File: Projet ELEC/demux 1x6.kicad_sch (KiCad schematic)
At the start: 4 parts, among them U1 74LS04, U2 74LS21, U3 74LS21, U4 74LS21

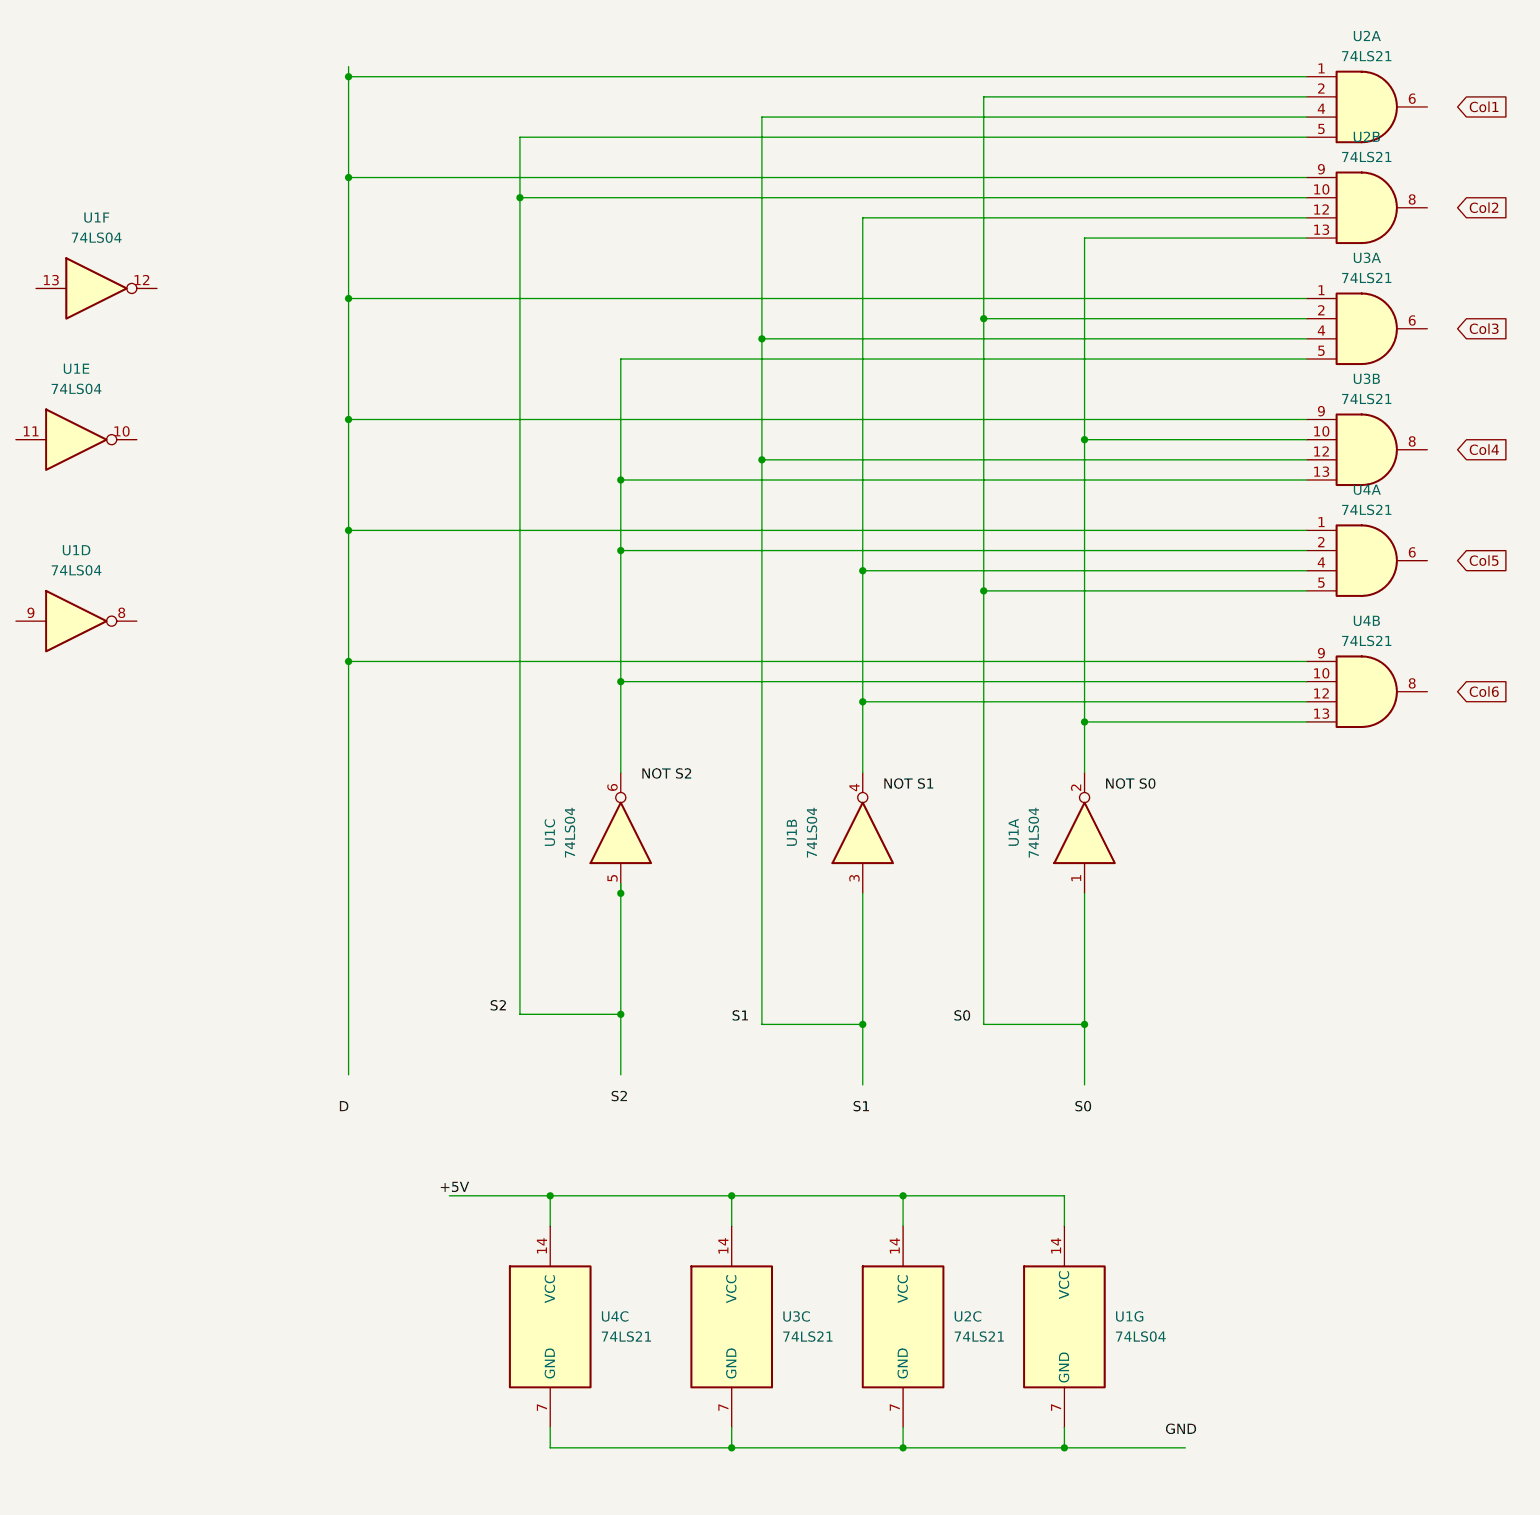
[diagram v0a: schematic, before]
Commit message: corrected around 60 errors, removed a 74ls04, and many other improvements
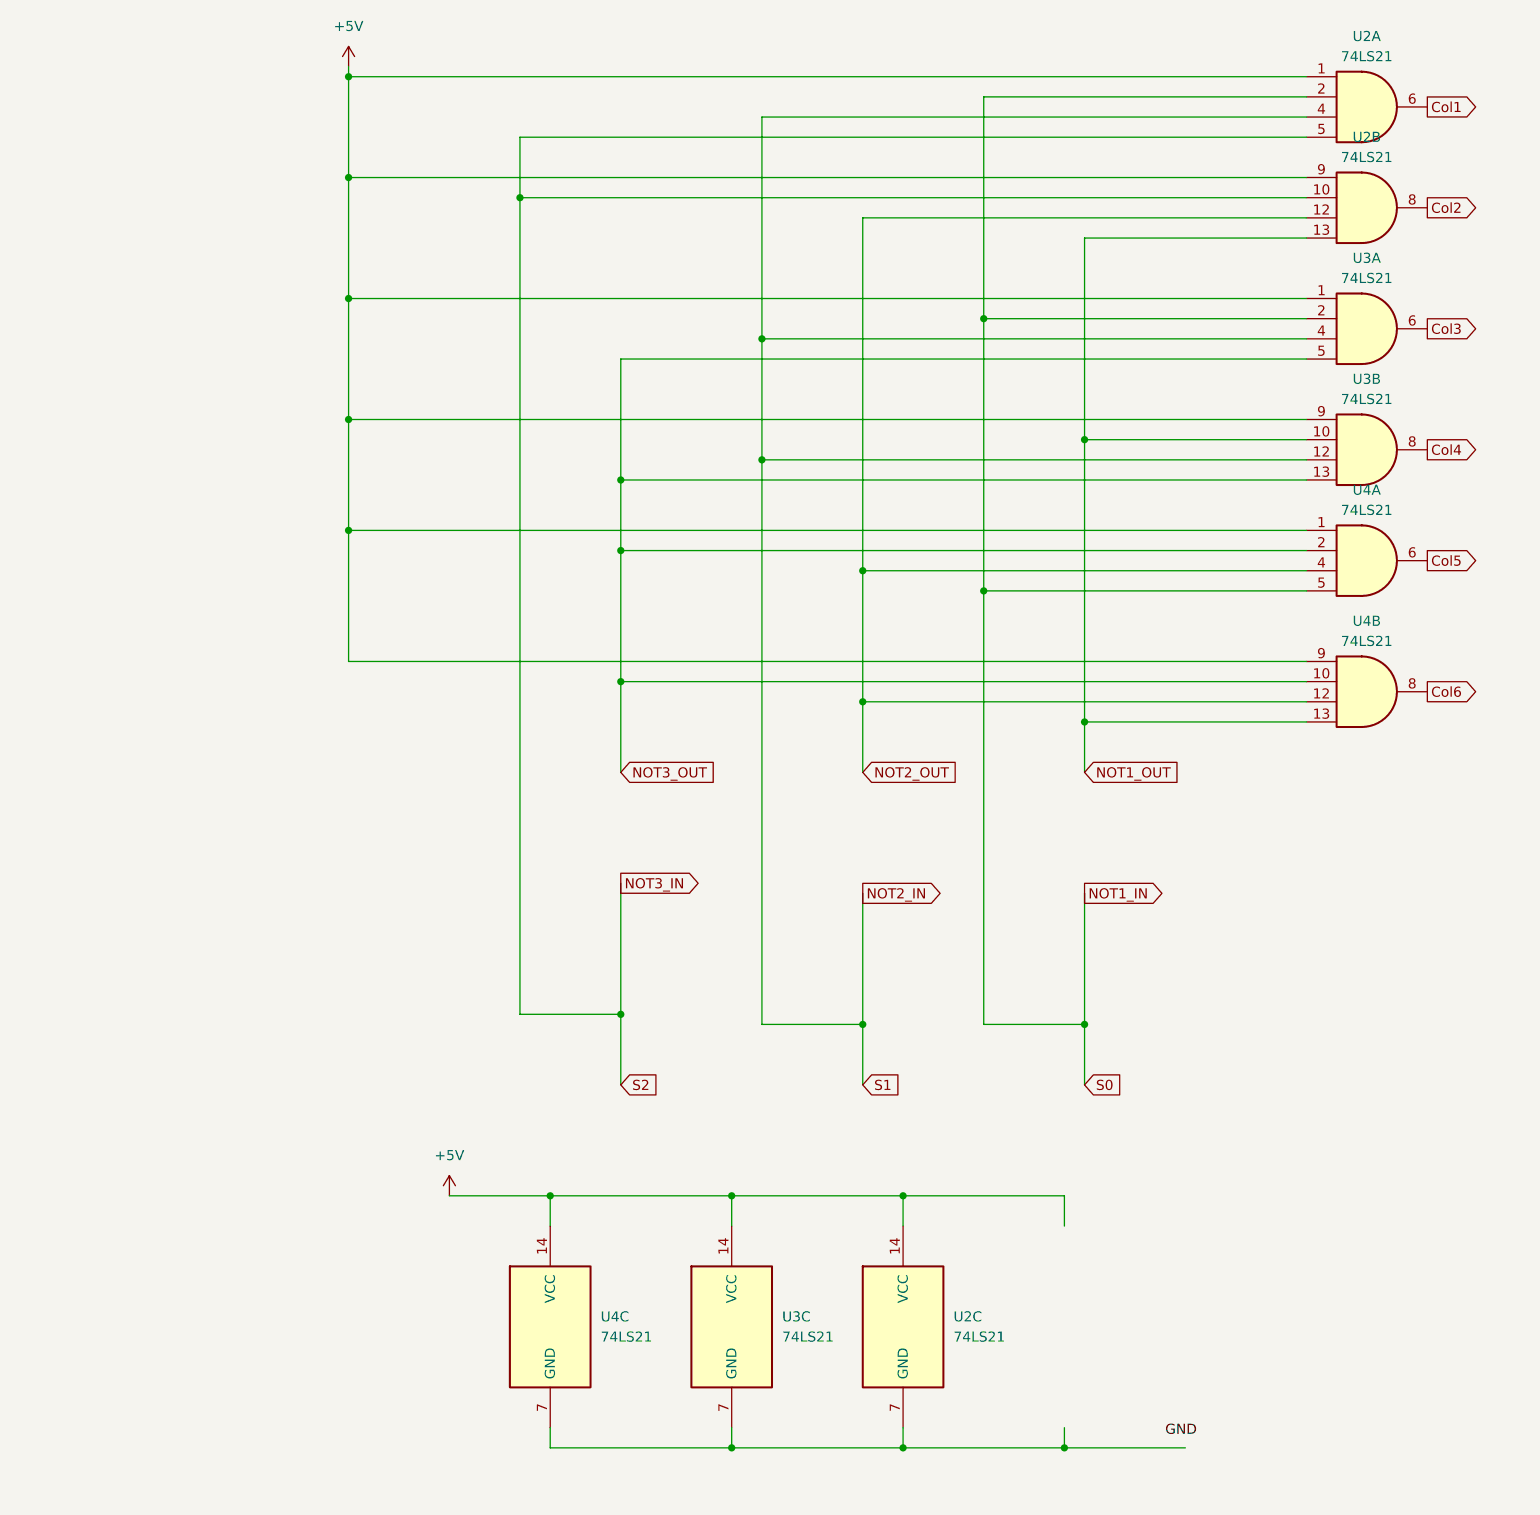
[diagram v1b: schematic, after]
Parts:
- removed U1: 74LS04, symbol 74xx:74LS04
- U2, U3, U4: footprint (none) -> Package_DIP:DIP-14_W7.62mm
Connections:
- net +5V: now also U2.1, U2.14 (VCC), U2.9, U3.1, U3.14 (VCC), U3.9, U4.1, U4.14 (VCC), U4.9
- net Col1: now also U2.6
- net Col2: now also U2.8
- net Col3: now also U3.6
- net Col4: now also U3.8
- net Col5: now also U4.6
- net Col6: now also U4.8
- net NOT1_OUT: now reaches U2.13, U3.10, U4.13
- net NOT2_IN: now reaches U2.4, U3.12, U3.4
- net NOT3_OUT: now reaches U3.13, U3.5, U4.10, U4.2
- net NOT2_OUT: now reaches U2.12, U4.12, U4.4
- net NOT1_IN: now reaches U2.2, U3.2, U4.5
- net NOT3_IN: now reaches U2.10, U2.5

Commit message: chore: update project to latest version (what's the point of git)
* Projet ELEC/Projet ELEC.kicad_pcb
* Projet ELEC/Projet ELEC.kicad_sch
* Projet ELEC/demux 1x6.kicad_sch
* Projet ELEC/keyboard.kicad_sch
* Projet ELEC/mux 6x1.kicad_sch
* Projet ELEC/stm32.kicad_sch
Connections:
- net GND: now also U2.7 (GND), U3.7 (GND), U4.7 (GND)
- net +5V renamed +3.3V
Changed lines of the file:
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@@
 	(paper "A4")
 	(junction
-		(at 156.21 189.23)
-		(diameter 0)
-		(color 0 0 0 0)
-	)
-	(junction
 		(at 66.04 59.69)
 		(diameter 0)
@@
 	)
 	(junction
-		(at 135.89 157.48)
-		(diameter 0)
-		(color 0 0 0 0)
-	)
-	(junction
 		(at 100.33 134.62)
 		(diameter 0)
@@
 	(wire
 		(pts
-			(xy 135.89 189.23) (xy 156.21 189.23)
+			(xy 135.89 189.23) (xy 170.18 189.23)
 		)
 		(stroke
@@
 	(wire
 		(pts
-			(xy 156.21 161.29) (xy 156.21 157.48)
-		)
-		(stroke
-			(width 0)
-			(type default)
-		)
-	)
-	(wire
-		(pts
-			(xy 156.21 186.69) (xy 156.21 189.23)
-		)
-		(stroke
-			(width 0)
-			(type default)
-		)
-	)
-	(wire
-		(pts
 			(xy 186.69 36.83) (xy 158.75 36.83)
 		)
@@
 	(wire
 		(pts
-			(xy 156.21 189.23) (xy 171.45 189.23)
-		)
-		(stroke
-			(width 0)
-			(type default)
-		)
-	)
-	(wire
-		(pts
 			(xy 66.04 73.66) (xy 66.04 90.17)
 		)
@@
 	(wire
 		(pts
-			(xy 135.89 157.48) (xy 156.21 157.48)
-		)
-		(stroke
-			(width 0)
-			(type default)
-		)
-	)
-	(wire
-		(pts
 			(xy 158.75 36.83) (xy 158.75 62.23)
 		)
@@
 			(width 0)
 			(type default)
-		)
-	)
-	(label "GND"
-		(at 168.91 187.96 0)
-		(fields_autoplaced yes)
-		(effects
-			(font
-				(size 1.27 1.27)
-			)
-			(justify left bottom)
 		)
 	)
@@
 			)
 		)
-		(property "Value" "+5V"
-			(at 66.04 10.16 0)
-			(effects
-				(font
-					(size 1.27 1.27)
-				)
+		(property "Value" "+3.3V"
+			(at 68.58 13.9699 0)
+			(effects
+				(font
+					(size 1.27 1.27)
+				)
+				(justify left)
 			)
 		)
@@
 				(path "/2d0c4a09-24e5-4892-bf2e-0a851a14e0ff/4d0d6547-4be3-42c7-87d5-a2ecca8bf422"
 					(reference "#PWR014")
+					(unit 1)
+				)
+			)
+		)
+	)
+	(symbol
+		(lib_id "power:GND")
+		(at 170.18 189.23 0)
+		(unit 1)
+		(exclude_from_sim no)
+		(in_bom yes)
+		(on_board yes)
+		(dnp no)
+		(fields_autoplaced yes)
+		(property "Reference" "#PWR012"
+			(at 170.18 195.58 0)
+			(effects
+				(font
+					(size 1.27 1.27)
+				)
+				(hide yes)
+			)
+		)
+		(property "Value" "GND"
+			(at 170.18 194.31 0)
+			(effects
+				(font
+					(size 1.27 1.27)
+				)
+			)
+		)
+		(property "Footprint" ""
+			(at 170.18 189.23 0)
+			(effects
+				(font
+					(size 1.27 1.27)
+				)
+				(hide yes)
+			)
+		)
+		(property "Datasheet" ""
+			(at 170.18 189.23 0)
+			(effects
+				(font
+					(size 1.27 1.27)
+				)
+				(hide yes)
+			)
+		)
+		(property "Description" "Power symbol creates a global label with name \"GND\" , ground"
+			(at 170.18 189.23 0)
+			(effects
+				(font
+					(size 1.27 1.27)
+				)
+				(hide yes)
+			)
+		)
+		(pin "1"
+		)
+		(instances
+			(project "Projet ELEC"
+				(path "/2d0c4a09-24e5-4892-bf2e-0a851a14e0ff/4d0d6547-4be3-42c7-87d5-a2ecca8bf422"
+					(reference "#PWR012")
 					(unit 1)
 				)
@@
 			)
 		)
-		(property "Value" "+5V"
+		(property "Value" "+3.3V"
 			(at 78.74 152.4 0)
 			(effects
